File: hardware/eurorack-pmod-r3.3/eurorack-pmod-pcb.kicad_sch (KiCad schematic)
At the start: 24 parts, among them Q1 2N7002E, U1 AK4619VN AUDIO CODEC, U2 TL074 OP AMP, U3 TL074 OP AMP, U4 PCA9557PW IO EXPANDER, U5 24AA025UIDT EEPROM, U7 CY8CMBR3116

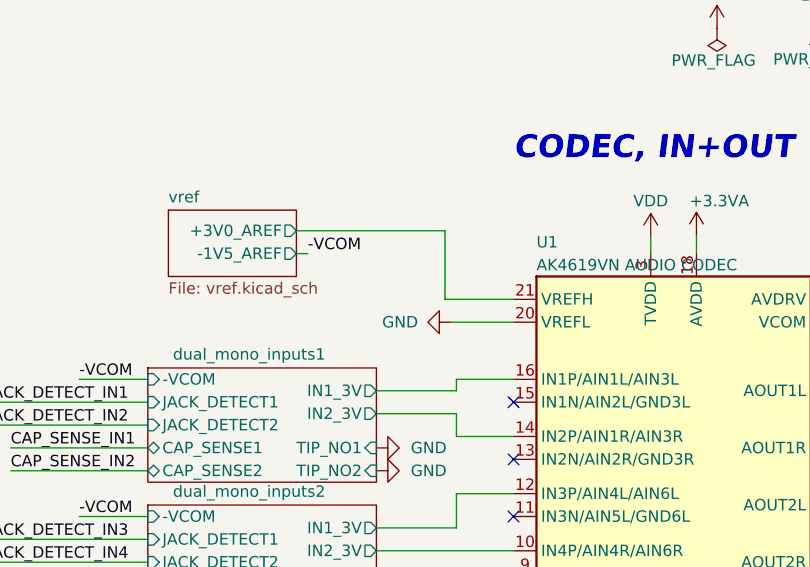
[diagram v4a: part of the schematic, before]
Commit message: vref: replace +3.0V with local 12V->3.3V LDO
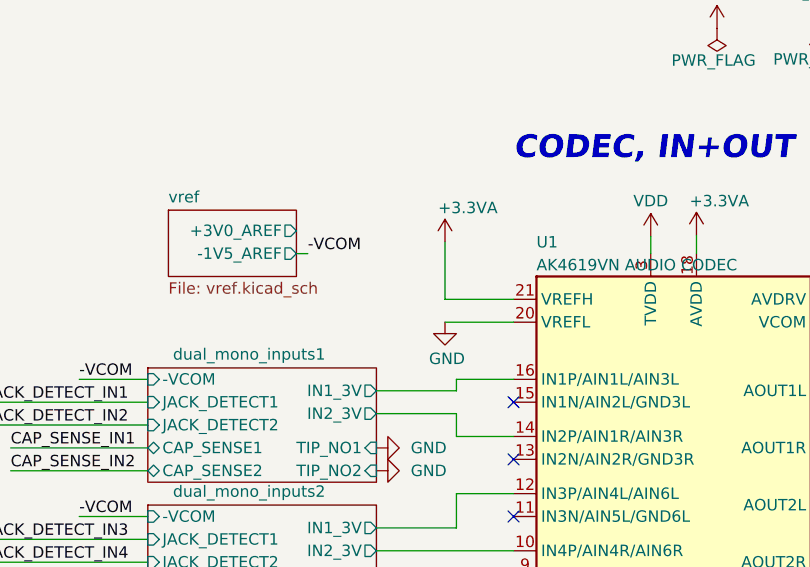
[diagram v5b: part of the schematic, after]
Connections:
- net +3.3VA: now also U1.21 (VREFH)
- net vref/+3V0_AREF: no longer U1.21 (VREFH)
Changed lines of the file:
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@@
 		)
 	)
+	(wire
+		(pts
+			(xy 177.8 41.91) (xy 177.8 48.26)
+		)
+		(stroke
+			(width 0)
+			(type default)
+		)
+	)
 	(polyline
 		(pts
@@
 	(wire
 		(pts
-			(xy 185.42 48.26) (xy 177.8 48.26)
-		)
-		(stroke
-			(width 0)
-			(type default)
-		)
-	)
-	(wire
-		(pts
 			(xy 180.975 96.52) (xy 185.42 96.52)
 		)
@@
 	(wire
 		(pts
+			(xy 177.8 48.26) (xy 185.42 48.26)
+		)
+		(stroke
+			(width 0)
+			(type default)
+		)
+	)
+	(wire
+		(pts
 			(xy 283.21 100.33) (xy 271.78 100.33)
 		)
@@
 	(wire
 		(pts
-			(xy 177.8 40.64) (xy 161.29 40.64)
-		)
-		(stroke
-			(width 0)
-			(type default)
-		)
-	)
-	(wire
-		(pts
 			(xy 129.54 80.01) (xy 144.78 80.01)
 		)
@@
 	(wire
 		(pts
-			(xy 178.435 50.8) (xy 185.42 50.8)
+			(xy 177.8 50.8) (xy 185.42 50.8)
 		)
 		(stroke
@@
 		)
 	)
-	(wire
-		(pts
-			(xy 177.8 48.26) (xy 177.8 40.64)
-		)
-		(stroke
-			(width 0)
-			(type default)
-		)
-	)
 	(label "JACK_DETECT_OUT1"
 		(at 141.605 172.085 0)
@@
 	)
 	(symbol
+		(lib_id "power:+3.3VA")
+		(at 177.8 41.91 0)
+		(unit 1)
+		(exclude_from_sim no)
+		(in_bom yes)
+		(on_board yes)
+		(dnp no)
+		(property "Reference" "#PWR020"
+			(at 177.8 45.72 0)
+			(effects
+				(font
+					(size 1.27 1.27)
+				)
+				(hide yes)
+			)
+		)
+		(property "Value" "+3.3VA"
+			(at 180.34 38.1 0)
+			(effects
+				(font
+					(size 1.27 1.27)
+				)
+			)
+		)
+		(property "Footprint" ""
+			(at 177.8 41.91 0)
+			(effects
+				(font
+					(size 1.27 1.27)
+				)
+				(hide yes)
+			)
+		)
+		(property "Datasheet" ""
+			(at 177.8 41.91 0)
+			(effects
+				(font
+					(size 1.27 1.27)
+				)
+				(hide yes)
+			)
+		)
+		(property "Description" ""
+			(at 177.8 41.91 0)
+			(effects
+				(font
+					(size 1.27 1.27)
+				)
+			)
+		)
+		(pin "1"
+		)
+		(instances
+			(project "eurorack-pmod-pcb"
+				(path "/d1469efb-590b-4a61-a37b-5bbc286936ba"
+					(reference "#PWR020")
+					(unit 1)
+				)
+			)
+		)
+	)
+	(symbol
 		(lib_id "Amplifier_Operational:TL074")
 		(at 158.75 101.6 0)
@@
 	(symbol
 		(lib_id "power:GND")
-		(at 178.435 50.8 270)
+		(at 177.8 50.8 0)
 		(unit 1)
 		(exclude_from_sim no)
@@
 		(dnp no)
 		(property "Reference" "#PWR023"
-			(at 172.085 50.8 0)
+			(at 177.8 57.15 0)
 			(effects
 				(font
@@
 		)
 		(property "Value" "GND"
-			(at 170.815 50.8 90)
+			(at 176.022 54.864 0)
 			(effects
 				(font
@@
 		)
 		(property "Footprint" ""
-			(at 178.435 50.8 0)
+			(at 177.8 50.8 0)
 			(effects
 				(font
@@
 		)
 		(property "Datasheet" ""
-			(at 178.435 50.8 0)
+			(at 177.8 50.8 0)
 			(effects
 				(font
@@
 		)
 		(property "Description" ""
-			(at 178.435 50.8 0)
+			(at 177.8 50.8 0)
 			(effects
 				(font

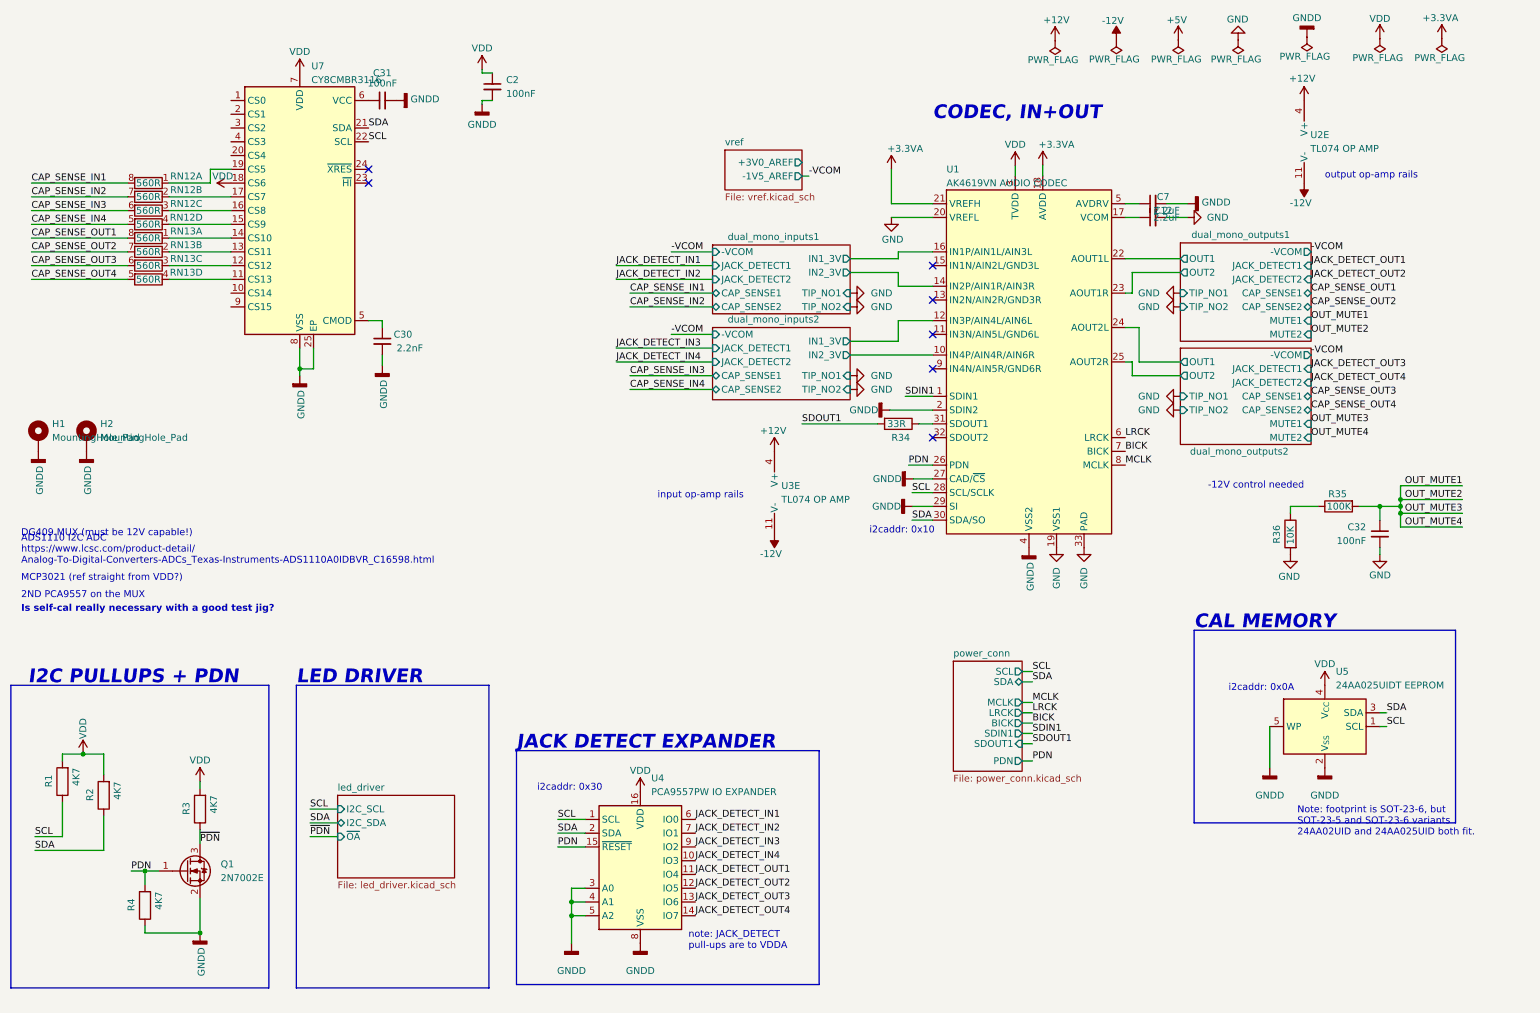
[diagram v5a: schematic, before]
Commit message: PDN/UNMUTE: add reset IC to PDN, swap PDN/UNMUTE ingress, add opto to UNMUTE
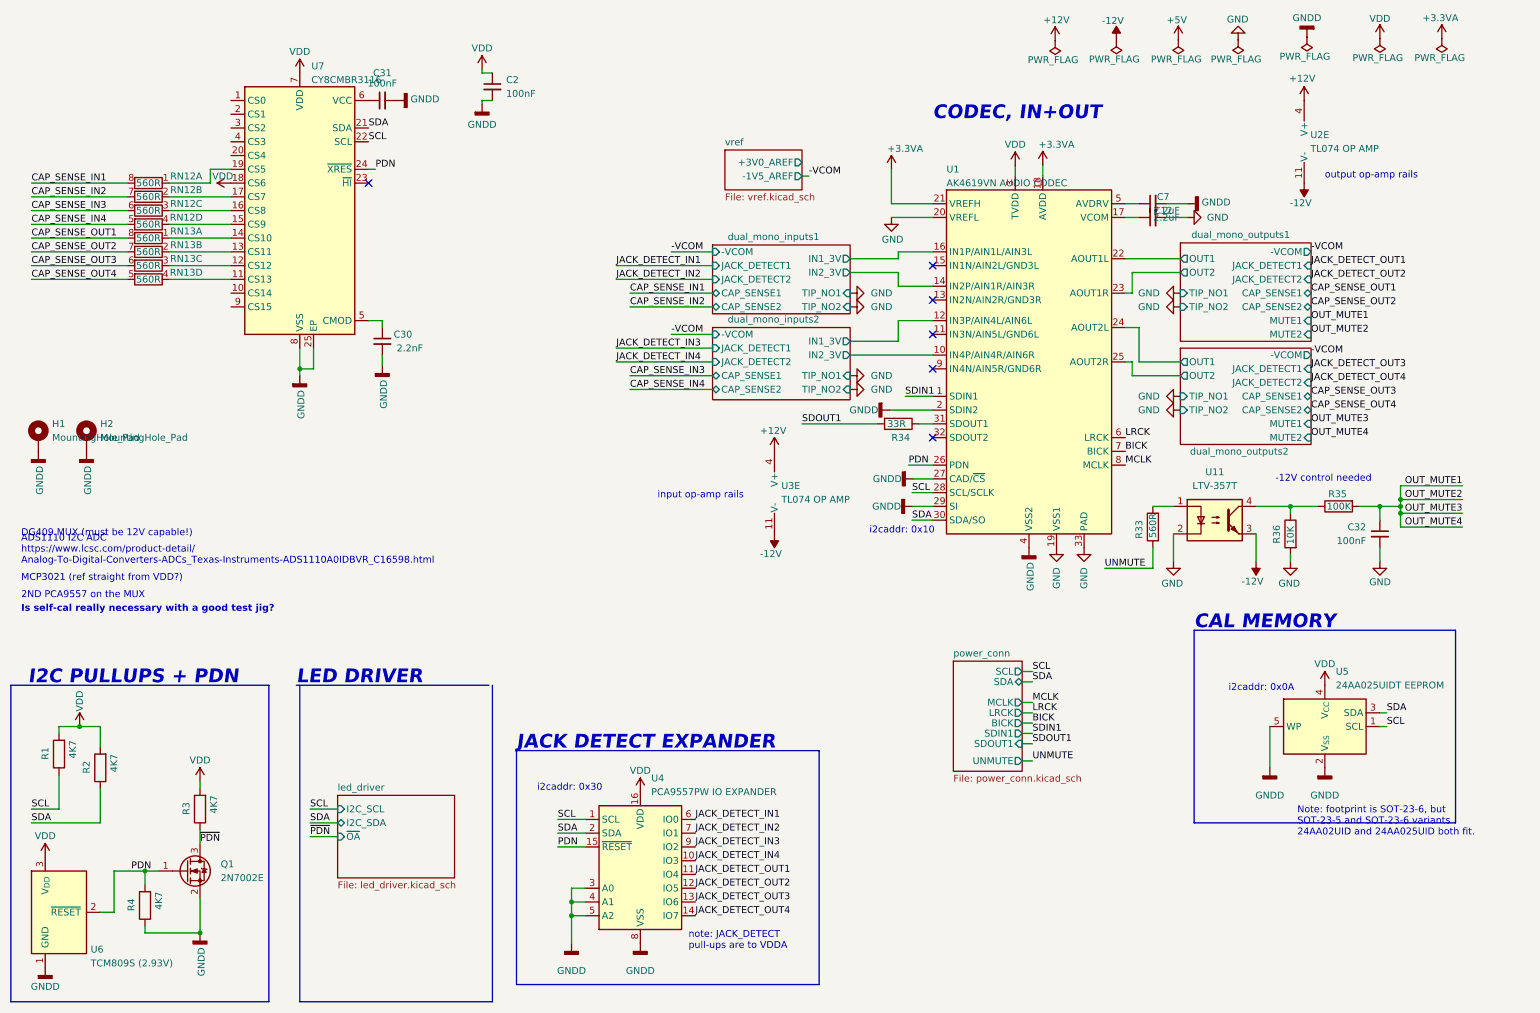
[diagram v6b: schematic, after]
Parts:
- added R33: 560R, Resistor_SMD:R_0402_1005Metric, symbol Device:R
- added U11: LTV-357T, Package_SO:SO-4_4.4x3.6mm_P2.54mm, symbol Isolator:LTV-357T
- added U6: TCM809S (2.93V), Package_TO_SOT_SMD:SOT-23, symbol Power_Supervisor:TCM809
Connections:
- net -12V: now also U11.3
- net GND: now also U11.2
- net GNDD: now also U6.1 (GND)
- net PDN: now also U7.24 (~{XRES}), U6.2 (~{RESET})
- net VDD: now also U6.3 (V_{DD})
- net at R35.1, R36.1: now also U11.4
- new net: R33.2, U11.1
- new net UNMUTE: R33.1
- no-connect marks 7 -> 6
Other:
- sheet power_conn ports: added UNMUTE; removed PDN
- moved on the sheet: R1, R2

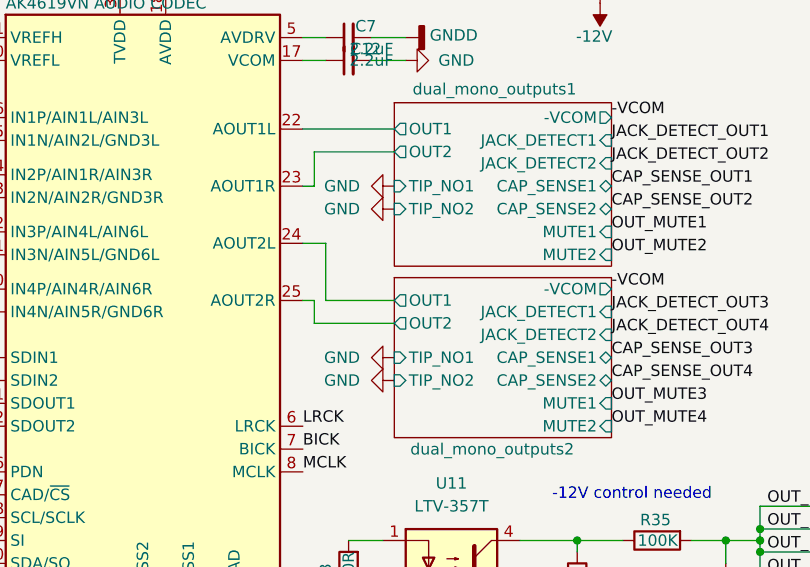
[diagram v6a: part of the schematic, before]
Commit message: r3.5: add 100k output terminations and 100nF vref filtering, fab outputs (not sent yet)
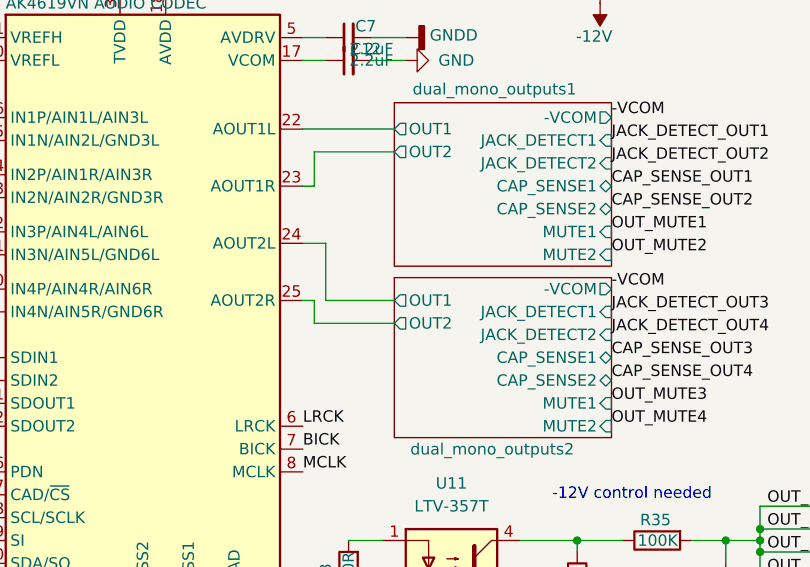
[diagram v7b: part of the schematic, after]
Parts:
- R33: LCSC (none) -> C25117
- R34: LCSC (none) -> C25105
- R35: LCSC (none) -> C25741
- R36: LCSC (none) -> C25744
- U1: LCSC (none) -> C3034747
- U11: LCSC (none) -> C33068
- U7: LCSC (none) -> C914913
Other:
- sheet dual_mono_outputs1 ports: added none; removed TIP_NO1, TIP_NO2
- sheet dual_mono_outputs2 ports: added none; removed TIP_NO1, TIP_NO2

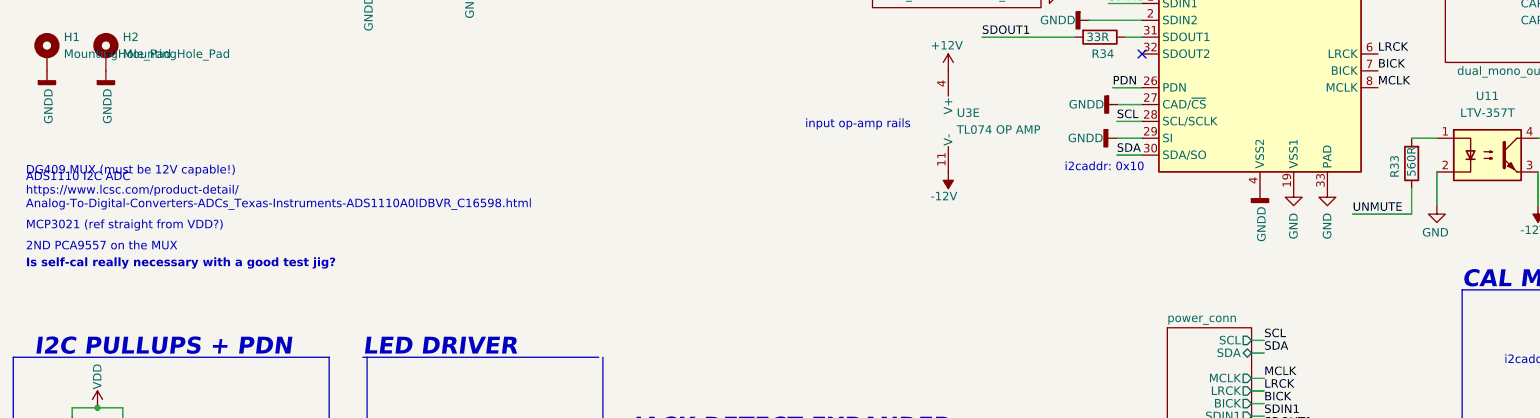
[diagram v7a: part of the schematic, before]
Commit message: r3.5: update part numbers and fab
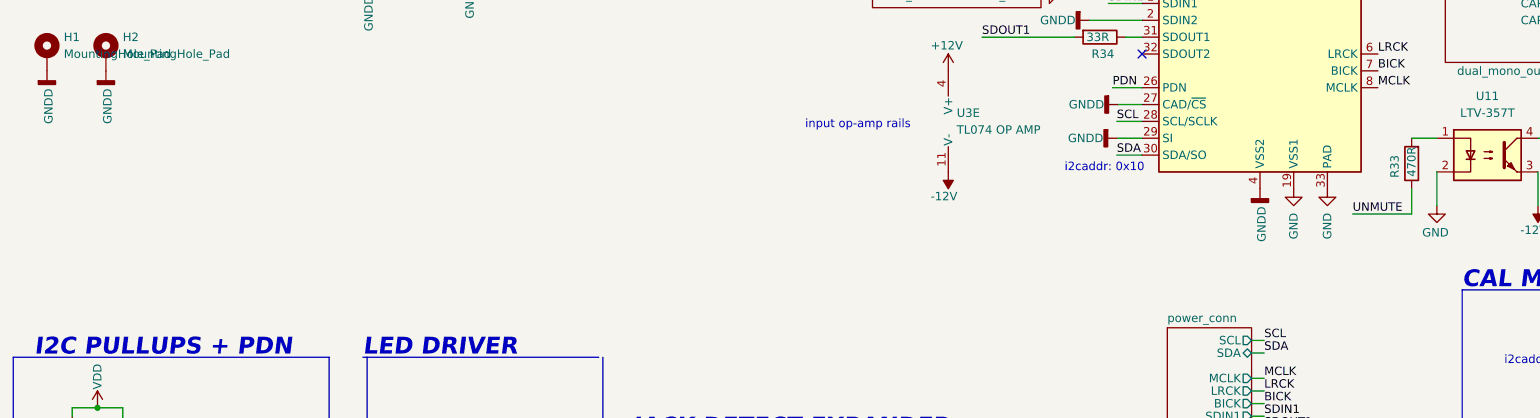
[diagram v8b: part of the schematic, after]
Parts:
- R33: value 560R -> 470R
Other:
- note removed: "2ND PCA9557 on the MUX"
- note removed: "ADS1110 I2C ADC https://www.lcsc.com/product-detail/ Analog-To-Digital-Converters-ADCs_Texas-Instruments-ADS1110A0IDBVR_C16598.html"
- note removed: "DG409 MUX (must be 12V capable!)"
- note removed: "Is self-cal really necessary with a good test jig?"
- note removed: "MCP3021 (ref straight from VDD?)"
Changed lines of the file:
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@@
-		)
-	)
-	(text "2ND PCA9557 on the MUX"
-		(exclude_from_sim no)
-		(at 17.145 121.285 0)
-		(effects
-			(font
-				(size 1.27 1.27)
-			)
-			(justify left bottom)
 		)
 	)
@@
 		)
 	)
-	(text "ADS1110 I2C ADC\nhttps://www.lcsc.com/product-detail/\nAnalog-To-Digital-Converters-ADCs_Texas-Instruments-ADS1110A0IDBVR_C16598.html"
-		(exclude_from_sim no)
-		(at 17.145 114.935 0)
-		(effects
-			(font
-				(size 1.27 1.27)
-			)
-			(justify left bottom)
-		)
-	)
 	(text "i2caddr: 0x30"
 		(exclude_from_sim no)
@@
 		)
 	)
-	(text "MCP3021 (ref straight from VDD?)"
-		(exclude_from_sim no)
-		(at 17.145 118.11 0)
-		(effects
-			(font
-				(size 1.27 1.27)
-			)
-			(justify left bottom)
-		)
-	)
 	(text "-12V control needed"
 		(exclude_from_sim no)
@@
 				(size 1.27 1.27)
 			)
-		)
-	)
-	(text "Is self-cal really necessary with a good test jig?"
-		(exclude_from_sim no)
-		(at 17.145 123.825 0)
-		(effects
-			(font
-				(size 1.27 1.27)
-				(thickness 0.254)
-				(bold yes)
-			)
-			(justify left bottom)
-		)
-	)
-	(text "DG409 MUX (must be 12V capable!)"
-		(exclude_from_sim no)
-		(at 17.145 109.855 0)
-		(effects
-			(font
-				(size 1.27 1.27)
-			)
-			(justify left bottom)
 		)
 	)
@@
 			)
 		)
-		(property "Value" "560R"
+		(property "Value" "470R"
 			(at 226.06 105.41 90)
 			(effects
